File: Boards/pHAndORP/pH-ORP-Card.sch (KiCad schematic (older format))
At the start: 118 parts, among them IC1 PIC32MM0064GPM028, P1 1x6 2.54 Pin Header, P2 AquaPicBus, P3 1x2 2.54, P4 BNC, P5 BNC, Q1 NX7002AK, Q2 NX7002AK, Q3 NX7002AK, Q4 AO3407A, Q5 MMBT3904, Q6 MMBT3904, Q7 AO3407A, Q8 AO3407A, U1 AP2114H, U10 LTC2483, U11 Si8602, U12 TC7660, U2 ST485EC, U3 LMC6061, U4 TLV272, U5 LTC2483, U6 Si8602, U7 TC7660, U8 LMC6061, U9 TLV272, X1 8MHz

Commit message: changed power supply isolation to n channel mosfet, schematic is now bom
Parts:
- removed Q5, Q6: MMBT3904, TO_SOT_Packages_SMD:SOT-23, symbol Q_NPN_BEC
- removed Q7, Q8: AO3407A, TO_SOT_Packages_SMD:SOT-23, symbol MOSFET_P_SMALL
- removed R45: 10K, Resistors_SMD:R_0805, symbol R
- added Q5, Q6: NX7002AK, TO_SOT_Packages_SMD:SOT-23, symbol GoodtimeDev:MOSFET_N_SMALL
- added R45: 10K, Resistors_SMD:R_0805, symbol pH-ORP-Card-rescue:R
- C1, C2, C3: symbol C_Small -> pH-ORP-Card-rescue:C_Small; Comments (none) -> 0805, 50V, X7R, 10%; Digi-Key Part Number (none) -> 445-7534-1-ND; Manufacturer (none) -> TDK; Manufacturer Part Number (none) -> C2012X7R1H104K085AA
- C10, C11, C12, C14, C15, C16, C21, C23, C24, C25, C26, C28, C29, C30, C6, C7, C9: symbol C -> pH-ORP-Card-rescue:C; Comments (none) -> 0805, 50V, X7R, 10%; Digi-Key Part Number (none) -> 445-7534-1-ND; Manufacturer (none) -> TDK; Manufacturer Part Number (none) -> C2012X7R1H104K085AA
- C13, C27: symbol C -> pH-ORP-Card-rescue:C; Comments (none) -> 0805, 25V, X7R, 10%; Digi-Key Part Number (none) -> 1276-1066-1-ND; Manufacturer (none) -> Samsung; Manufacturer Part Number (none) -> CL21B105KAFNNNE
- C17, C20, C31, C34: symbol CP1 -> pH-ORP-Card-rescue:CP1; Comments (none) -> 0805, 10V, X7R, 10%; Digi-Key Part Number (none) -> 490-10516-1-ND; Manufacturer (none) -> Murata; Manufacturer Part Number (none) -> GRM21BR71A106KA73L
- C18, C32: symbol C -> pH-ORP-Card-rescue:C; Comments (none) -> 0805, 10V, X7R, 10%; Digi-Key Part Number (none) -> 1276-2972-1-ND; Manufacturer (none) -> Samsung; Manufacturer Part Number (none) -> CL21B475KPFNNNE
- C19, C33: symbol C -> pH-ORP-Card-rescue:C; Comments (none) -> 0805, 10V, X7R, 10%; Digi-Key Part Number (none) -> 490-10516-1-ND; Manufacturer (none) -> Murata; Manufacturer Part Number (none) -> GRM21BR71A106KA73L
- C22, C8: symbol C -> pH-ORP-Card-rescue:C; Comments (none) -> 0805, 50V, C0G/NP0, 10%; Digi-Key Part Number (none) -> 399-8062-1-ND; Manufacturer (none) -> Kemet; Manufacturer Part Number (none) -> C0805C330K5GACTU
- C4, C5: symbol C_Small -> pH-ORP-Card-rescue:C_Small; Comments (none) -> 0805, 10V, X7R, 10%; Digi-Key Part Number (none) -> 1276-2972-1-ND; Manufacturer (none) -> Samsung; Manufacturer Part Number (none) -> CL21B475KPFNNNE
- D1: symbol TRI-LED -> GoodtimeDev:TRI-LED; Comments (none) -> 4-PLCC; Digi-Key Part Number (none) -> 492-2173-1-ND; Manufacturer (none) -> Bivar; Manufacturer Part Number (none) -> SMTL4-RGY
- D2: symbol LED_ALT -> pH-ORP-Card-rescue:LED_ALT; Comments (none) -> 0805, 2V, 20mA; Digi-Key Part Number (none) -> 475-1278-1-ND; Manufacturer (none) -> Osram; Manufacturer Part Number (none) -> LS R976-NR-1
- D3, D4: symbol D_Schottky_ALT -> pH-ORP-Card-rescue:D_Schottky_ALT; Comments (none) -> SOD-323, 200mA; Digi-Key Part Number (none) -> DB2J31000LCT-ND; Manufacturer (none) -> Panasonic; Manufacturer Part Number (none) -> DB2J31000L
- IC1: symbol PIC32MM0064GPM028_QFN -> GoodtimeDev:PIC32MM0064GPM028_QFN; Comments (none) -> 28-QFN 6x6; Digi-Key Part Number (none) -> PIC32MM0064GPM028T-I/MLCT-ND; Manufacturer (none) -> Microchip; Manufacturer Part Number (none) -> PIC32MM0064GPM028T-I/ML
- P1: symbol CONN_01X06 -> pH-ORP-Card-rescue:CONN_01X06; Comments (none) -> -; Digi-Key Part Number (none) -> A105161CT-ND; Manufacturer (none) -> TE; Manufacturer Part Number (none) -> 5-146868-1
- P2: symbol USB1.0_Stacked -> GoodtimeDev:USB1.0_Stacked; Comments (none) -> -; Digi-Key Part Number (none) -> 1175-1003-ND; Manufacturer (none) -> CNC Tech; Manufacturer Part Number (none) -> 1001-004-01010
- P3: symbol CONN_01X02 -> pH-ORP-Card-rescue:CONN_01X02; Comments (none) -> -; Digi-Key Part Number (none) -> ED10561-ND; Manufacturer (none) -> On Shore; Manufacturer Part Number (none) -> OSTVN02A150
- P4, P5: symbol BNC -> pH-ORP-Card-rescue:BNC; Comments (none) -> -; Digi-Key Part Number (none) -> A97553-ND; Manufacturer (none) -> TE; Manufacturer Part Number (none) -> 1-1337543-0
- PS1, PS2: symbol ROE-0505S -> GoodtimeDev:ROE-0505S; Comments (none) -> 8-SMD Module, 5 Leads; Digi-Key Part Number (none) -> 945-1659-1-ND; Manufacturer (none) -> Recom; Manufacturer Part Number (none) -> R1SE-0505-R
- Q1, Q2, Q3: symbol MOSFET_N_SMALL -> GoodtimeDev:MOSFET_N_SMALL; Comments (none) -> SOT-23-3; Digi-Key Part Number (none) -> 1727-1289-6-ND; Manufacturer (none) -> Nexperia; Manufacturer Part Number (none) -> NX7002AK,215
- Q4: symbol MOSFET_P_SMALL -> GoodtimeDev:MOSFET_P_SMALL; Comments (none) -> SOT-23-3; Digi-Key Part Number (none) -> 785-1006-1-ND; Manufacturer (none) -> Alpha Omega; Manufacturer Part Number (none) -> AO3407A
- R1, R10, R11, R12, R2, R25, R26, R39, R40, R9: symbol R -> pH-ORP-Card-rescue:R; Comments (none) -> 0805, 1/4W, 1%, Thin Film; Digi-Key Part Number (none) -> RNCP0805FTD4K99CT-ND; Manufacturer (none) -> Stackpole; Manufacturer Part Number (none) -> RNCP0805FTD4K99
- R13, R3, R4, R5: symbol R -> pH-ORP-Card-rescue:R; Comments (none) -> 0805, 1/4W, 1%, Thin Film; Digi-Key Part Number (none) -> RNCP0805FTD150RCT-ND; Manufacturer (none) -> Stackpole; Manufacturer Part Number (none) -> RNCP0805FTD150R
- R14, R28: footprint Resistors_SMD:R_0805 -> MyFootPrints:R_Axial_DIN0207_L6.3mm_D2.5mm_P7.62mm_Horizontal; symbol R -> pH-ORP-Card-rescue:R; Comments (none) -> Axial, 1/4W, 1%, Metal Film; Digi-Key Part Number (none) -> RNF14FTD10K0CT-ND; Manufacturer (none) -> Stackpole; Manufacturer Part Number (none) -> RNF14FTD10K0
- R15, R29: symbol R -> pH-ORP-Card-rescue:R; Comments (none) -> 0805, 1/4W, 1%, Thin Film; Digi-Key Part Number (none) -> RMCF0805FT2M00CT-ND; Manufacturer (none) -> Stackpole; Manufacturer Part Number (none) -> RMCF0805FT2M00
- R16: symbol R -> pH-ORP-Card-rescue:R; Comments (none) -> 0805, 1/4W, 1%, Thin Film; Digi-Key Part Number (none) -> RNCP0805FTD49K9CT-ND; Manufacturer (none) -> Stackpole; Manufacturer Part Number (none) -> RNCP0805FTD49K9
- R17, R18, R19, R20, R21, R31, R32, R33, R34, R35: symbol R -> pH-ORP-Card-rescue:R; Comments (none) -> 0805, 1/4W, 1%, Thin Film; Digi-Key Part Number (none) -> RMCF0805FT221KCT-ND; Manufacturer (none) -> Stackpole; Manufacturer Part Number (none) -> RMCF0805FT221K
- R22, R36, R42, R43, R6: symbol R -> pH-ORP-Card-rescue:R; Comments (none) -> 0805, 1/4W, 1%, Thin Film; Digi-Key Part Number (none) -> RNCP0805FTD1K00CT-ND; Manufacturer (none) -> Stackpole; Manufacturer Part Number (none) -> RNCP0805FTD1K00
- R23, R24, R37, R38, R44, R7, R8: symbol R -> pH-ORP-Card-rescue:R; Comments (none) -> 0805, 1/4W, 1%, Thin Film; Digi-Key Part Number (none) -> RNCP0805FTD10K0CT-ND; Manufacturer (none) -> Stackpole; Manufacturer Part Number (none) -> RNCP0805FTD10K0
- R27, R41: symbol R -> pH-ORP-Card-rescue:R; Comments (none) -> 2512, 1W, 1%, Thick Film; Digi-Key Part Number (none) -> 541-49.9AFCT-ND; Manufacturer (none) -> Vishay Dale; Manufacturer Part Number (none) -> CRCW251249R9FKEG
- R30: symbol R -> pH-ORP-Card-rescue:R; Comments (none) -> 0805, 1/4W, 1%, Thin Film; Digi-Key Part Number (none) -> RMCF0805FT100KCT-ND; Manufacturer (none) -> Stackpole; Manufacturer Part Number (none) -> RMCF0805FT100K
- RV1, RV3: symbol POT -> pH-ORP-Card-rescue:POT; Comments (none) -> J Lead, 12T; Digi-Key Part Number (none) -> 987-1554-ND; Manufacturer (none) -> TT; Manufacturer Part Number (none) -> 84WR50KLF
- RV2, RV4: symbol POT -> pH-ORP-Card-rescue:POT; Comments (none) -> J Lead, 12T; Digi-Key Part Number (none) -> 987-1155-ND; Manufacturer (none) -> TT; Manufacturer Part Number (none) -> 84WR10KLF
- TP1, TP2: symbol TEST_1P -> pH-ORP-Card-rescue:TEST_1P
- U1: symbol AP1117-33 -> pH-ORP-Card-rescue:AP1117-33; Comments (none) -> SOT-223; Digi-Key Part Number (none) -> AP2114HA-2.5TRG1DICT-ND; Manufacturer (none) -> Diodes; Manufacturer Part Number (none) -> AP2114HA-2.5TRG1
- U10, U5: symbol LTC2483 -> GoodtimeDev:LTC2483; Comments (none) -> 10-DFN 3x3mm; Digi-Key Part Number (none) -> LTC2483CDD#PBF-ND; Manufacturer (none) -> Linear; Manufacturer Part Number (none) -> LTC2483CDD#PBF
- U11, U6: symbol Si8602 -> GoodtimeDev:Si8602; Comments (none) -> 8-SOIC 3.9mm; Digi-Key Part Number (none) -> SI8602AB-B-IS-ND; Manufacturer (none) -> Silicon Labs; Manufacturer Part Number (none) -> SI8602AB-B-IS
- U12, U7: symbol TC7660 -> GoodtimeDev:TC7660; Comments (none) -> 8-SOIC 3.9mm; Digi-Key Part Number (none) -> TC7660EOA-ND; Manufacturer (none) -> Microchip; Manufacturer Part Number (none) -> TC7660EOA
- U2: symbol SN75176B -> GoodtimeDev:SN75176B; Comments (none) -> 8-SOIC; Digi-Key Part Number (none) -> 497-3735-1-ND; Manufacturer (none) -> STMicro; Manufacturer Part Number (none) -> ST485ECDR
- U3, U8: symbol LMC6061 -> GoodtimeDev:LMC6061; Comments (none) -> 8-SOIC 3.9mm; Digi-Key Part Number (none) -> LMC6061AIMX/NOPBCT-ND; Manufacturer (none) -> Texas Instruments; Manufacturer Part Number (none) -> LMC6061AIMX/NOPB
- U4, U9: symbol LM358 -> pH-ORP-Card-rescue:LM358; Comments (none) -> 8-SOIC 3.9mm; Digi-Key Part Number (none) -> TLV272IS-13DICT-ND; Manufacturer (none) -> Diodes Inc; Manufacturer Part Number (none) -> TLV272IS-13
- X1: symbol RESONATOR -> GoodtimeDev:RESONATOR; Comments (none) -> 3-SMD, Non-Standard; Digi-Key Part Number (none) -> 490-1195-1-ND; Manufacturer (none) -> Murata; Manufacturer Part Number (none) -> CSTCE8M00G55-R0
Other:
- moved on the sheet: C17, C18, C19, C20, C31, C32, C33, C34, R27, R41, R42, R43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

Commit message: removed tracking bom and schematics
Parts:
- C1, C10, C11, C12, C13, C14, C15, C16, C17, C18, C19, C2, C20, C21, C22, C23, C24, C25, C26, C27, C28, C29, C3, C30, C31, C32, C33, C34, C4, C5, C6, C7, C8, C9: Type (none) -> Capacitor
- D1: Type (none) -> LED (Red, Green, Yellow)
- D2: Type (none) -> LED (Red)
- D3, D4: Type (none) -> Schottky Diode
- IC1: Type (none) -> Microcontroller
- P1: value 1x6 2.54 Pin Header -> ICSP; Type (none) -> 1x6 2.54 Male Pin Header
- P2: Type (none) -> USB 1.1 Type A
- P3: value 1x2 2.54 -> Power; Type (none) -> 1x2 2.54 Screw Header
- P4: value BNC -> pH; Type (none) -> BNC
- P5: value BNC -> pH/ORP; Type (none) -> BNC
- PS1, PS2: Type (none) -> 1W Isolated Power Supply
- Q1, Q2, Q3, Q5, Q6: Type (none) -> N-Channel MOSFET
- Q4: Type (none) -> P-Channel MOSFET
- R1, R10, R11, R12, R13, R14, R15, R16, R17, R18, R19, R2, R20, R21, R22, R23, R24, R25, R26, R27, R28, R29, R3, R30, R31, R32, R33, R34, R35, R36, R37, R38, R39, R4, R40, R41, R42, R43, R44, R45, R5, R6, R7, R8, R9: Type (none) -> Resistor
- RV1, RV2, RV3, RV4: Type (none) -> Potentiomenter
- TP1, TP2: Comments (none) -> -; Digi-Key Part Number (none) -> -; Manufacturer (none) -> -; Manufacturer Part Number (none) -> -; Type (none) -> -
- U1: Type (none) -> Linear Regulator
- U10, U5: Type (none) -> DeltaSigma ADC
- U11, U6: Type (none) -> I2C Isolator
- U12, U7: Type (none) -> Power Convertor
- U2: Type (none) -> RS485 Transceiver
- U3, U4, U8, U9: Type (none) -> OpAmp
- X1: Type (none) -> Resonator

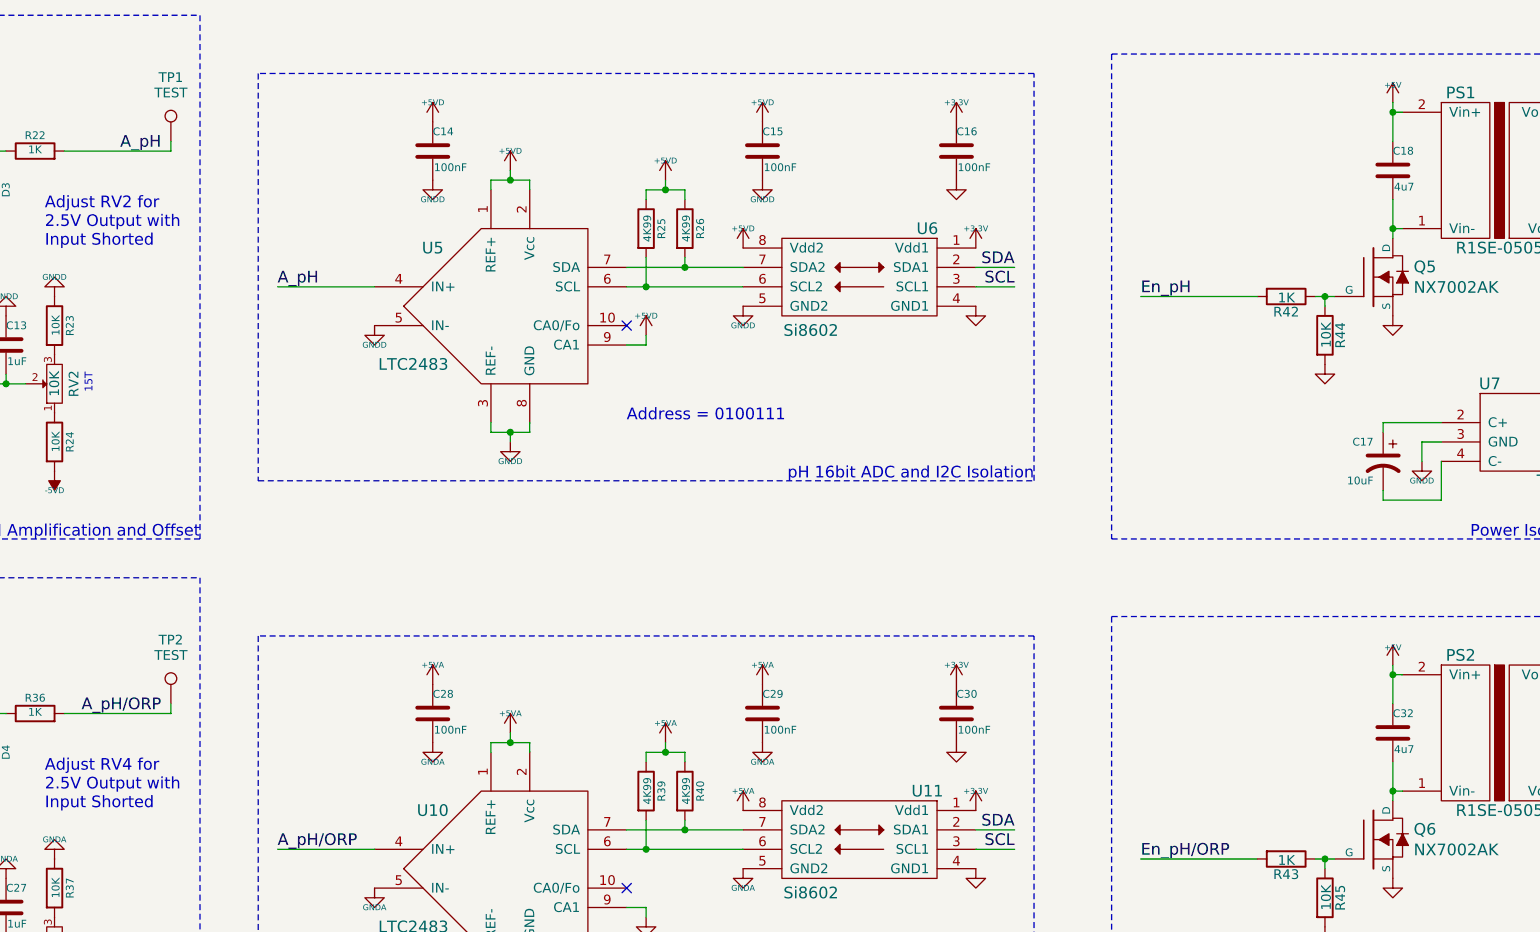
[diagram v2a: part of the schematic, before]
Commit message: changed power supply switch from p channel to n channel
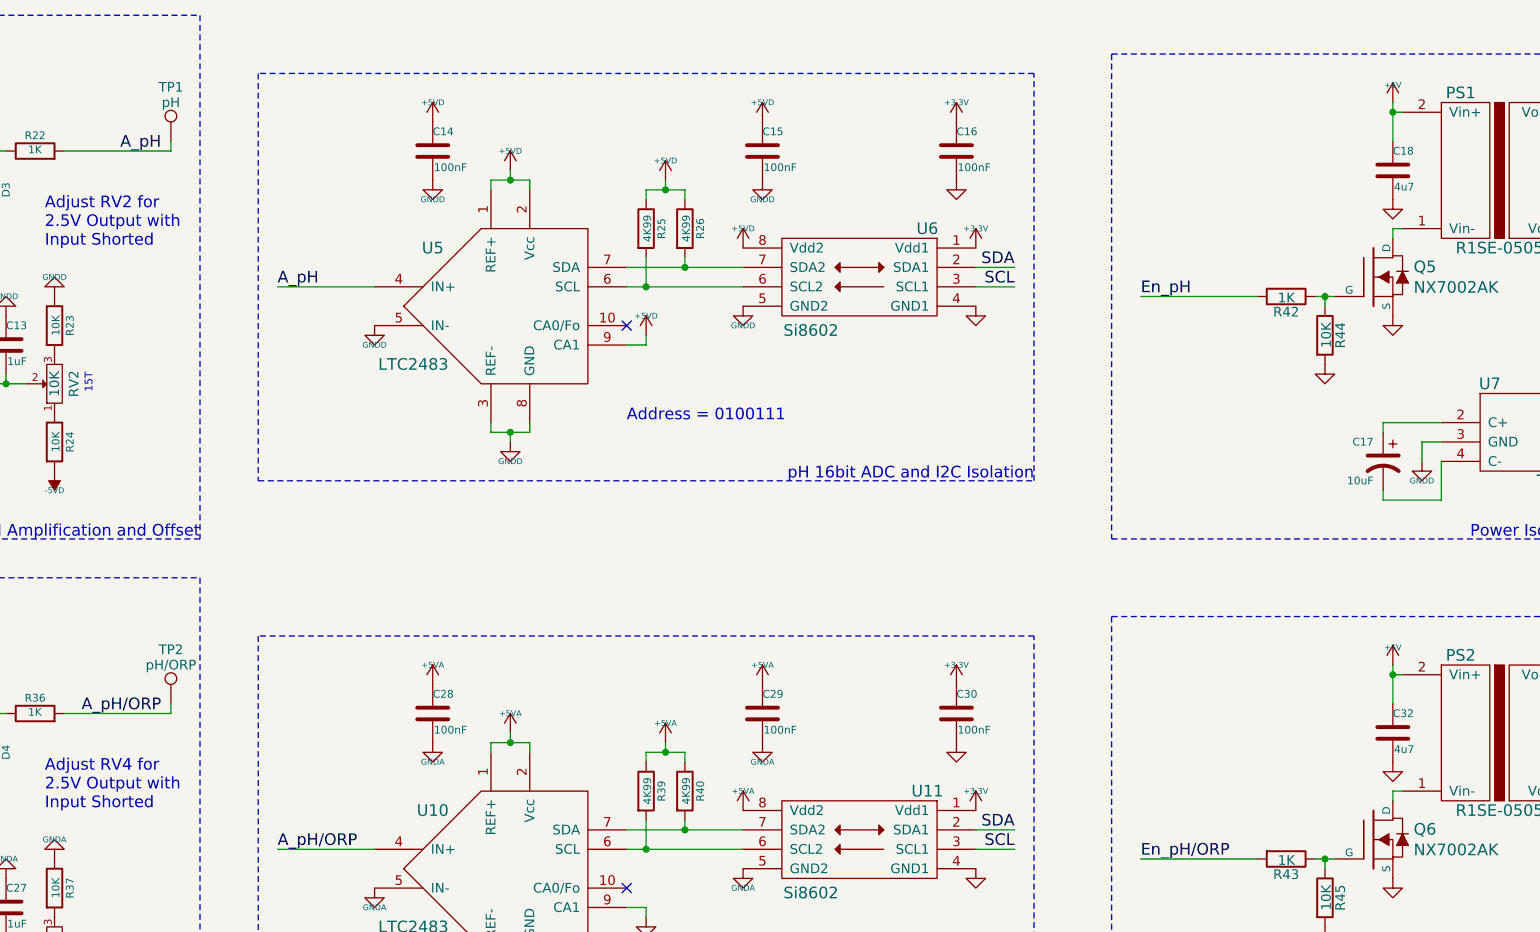
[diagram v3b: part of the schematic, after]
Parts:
- P1: footprint Pin_Headers:Pin_Header_Straight_1x06_Pitch2.54mm -> Connector_PinHeader_2.54mm:PinHeader_1x06_P2.54mm_Vertical
- TP1: value TEST -> pH; footprint Measurement_Points:Measurement_Point_Round-SMD-Pad_Small -> TestPoint:TestPoint_Pad_D1.5mm
- TP2: value TEST -> pH/ORP; footprint Measurement_Points:Measurement_Point_Round-SMD-Pad_Small -> TestPoint:TestPoint_Pad_D1.5mm
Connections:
- net GND: now also C18.2, C32.2
- net at PS1.1 (Vin-), Q5.3 (D): no longer C18.2
- net at PS2.1 (Vin-), Q6.3 (D): no longer C32.2
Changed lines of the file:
@@
 F 0 "P1" H 3950 8850 50  0000 C CNN
 F 1 "ICSP" V 4050 8500 50  0001 C CNN
-F 2 "Pin_Headers:Pin_Header_Straight_1x06_Pitch2.54mm" H 3950 8500 60  0001 C CNN
+F 2 "Connector_PinHeader_2.54mm:PinHeader_1x06_P2.54mm_Vertical" H 3950 8500 60  0001 C CNN
 F 3 "" H 3950 8500 60  0000 C CNN
 F 4 "-" H 0   0   50  0001 C CNN "Comments"
@@
 Wire Wire Line
 	7500 2300 7600 2300
-Connection ~ 11450 1700
 Wire Wire Line
 	11450 1700 11500 1700
 Wire Wire Line
-	11450 1550 11450 1700
-Wire Wire Line
 	11450 1700 11450 1750
 Connection ~ 11450 1100
@@
 U 1 1 5A296A71
 P 5150 1250
-F 0 "TP1" H 5150 1550 50  0000 C BNN
-F 1 "TEST" H 5150 1500 50  0000 C CNN
-F 2 "Measurement_Points:Measurement_Point_Round-SMD-Pad_Small" H 5150 1250 50  0001 C CNN
+F 0 "TP1" H 5150 1500 50  0000 C BNN
+F 1 "pH" H 5150 1450 50  0000 C CNN
+F 2 "TestPoint:TestPoint_Pad_D1.5mm" H 5150 1250 50  0001 C CNN
 F 3 "" H 5150 1250 50  0001 C CNN
 F 4 "-" H 0   0   50  0001 C CNN "Comments"
@@
 U 1 1 5A298C96
 P 5150 4150
-F 0 "TP2" H 5150 4450 50  0000 C BNN
-F 1 "TEST" H 5150 4400 50  0000 C CNN
-F 2 "Measurement_Points:Measurement_Point_Round-SMD-Pad_Small" H 5150 4150 50  0001 C CNN
+F 0 "TP2" H 5150 4400 50  0000 C BNN
+F 1 "pH/ORP" H 5150 4350 50  0000 C CNN
+F 2 "TestPoint:TestPoint_Pad_D1.5mm" H 5150 4150 50  0001 C CNN
 F 3 "" H 5150 4150 50  0001 C CNN
 F 4 "-" H 0   0   50  0001 C CNN "Comments"
@@
 	1    0    0    -1
 $EndComp
-Connection ~ 11450 4600
 Wire Wire Line
 	11450 4600 11500 4600
 Wire Wire Line
-	11450 4450 11450 4600
-Wire Wire Line
 	11450 4600 11450 4650
 Connection ~ 11450 4000
@@
 	1    0    0    -1
 $EndComp
+$Comp
+L power:GND #PWR?
+U 1 1 5BB39D3C
+P 11450 1550
+F 0 "#PWR?" H 11450 1550 30  0001 C CNN
+F 1 "GND" H 11450 1480 30  0001 C CNN
+F 2 "~" H 11450 1550 60  0001 C CNN
+F 3 "~" H 11450 1550 60  0000 C CNN
+	1    11450 1550
+	1    0    0    -1
+$EndComp
+$Comp
+L power:GND #PWR?
+U 1 1 5BB3EDF1
+P 11450 4450
+F 0 "#PWR?" H 11450 4450 30  0001 C CNN
+F 1 "GND" H 11450 4380 30  0001 C CNN
+F 2 "~" H 11450 4450 60  0001 C CNN
+F 3 "~" H 11450 4450 60  0000 C CNN
+	1    11450 4450
+	1    0    0    -1
+$EndComp
